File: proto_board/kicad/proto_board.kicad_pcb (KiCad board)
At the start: 2 copper layers, 91 x 96 mm, 1074 parts, among them J1 pcie_98

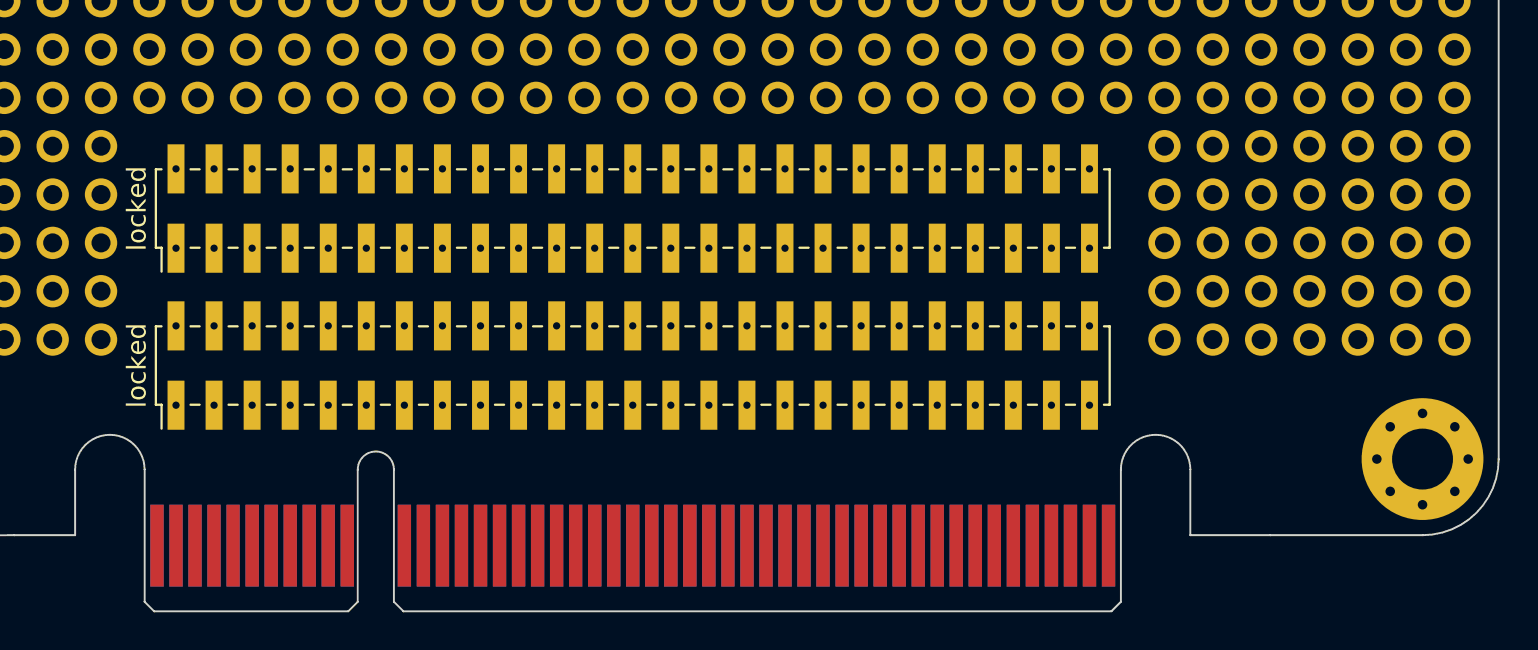
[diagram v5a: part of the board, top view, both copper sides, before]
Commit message: Proto board completed.
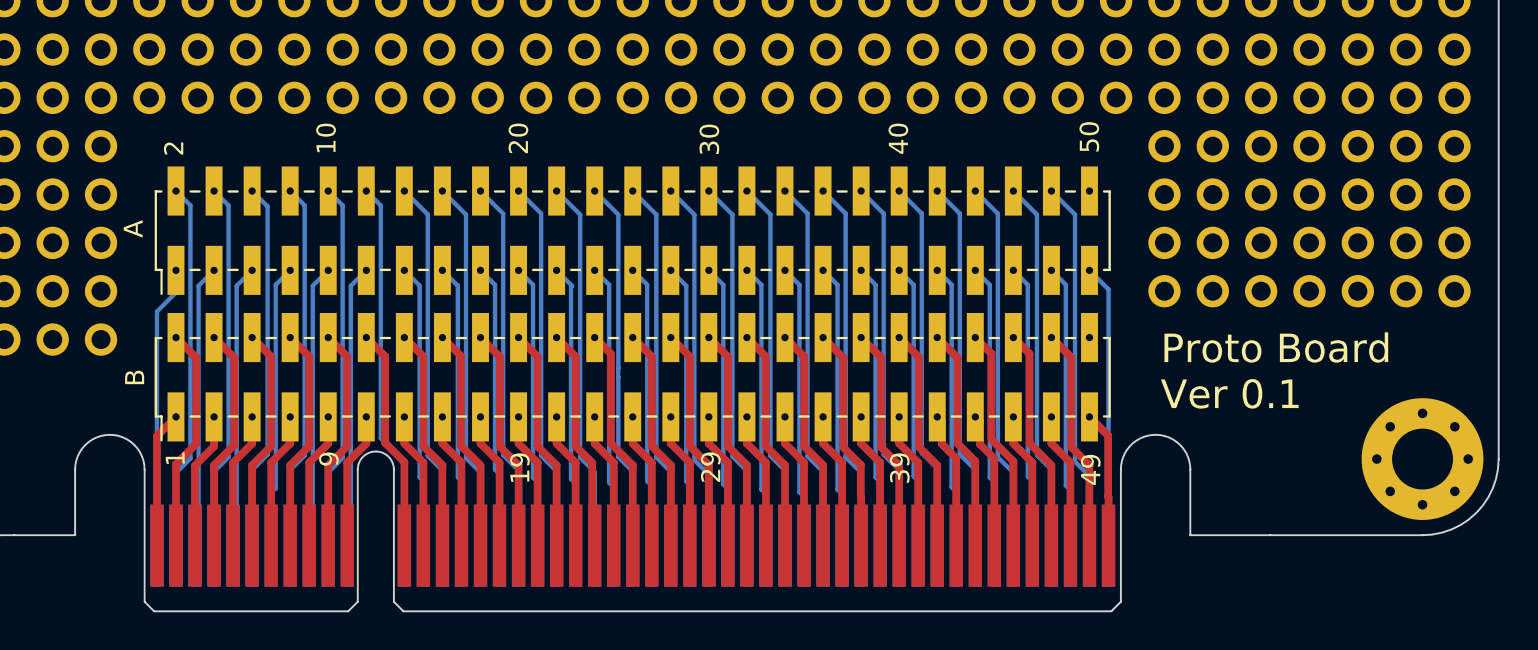
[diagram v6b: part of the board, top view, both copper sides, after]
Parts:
- removed the REF** at (56.7, -14.3)
- removed the REF** at (44.0, -14.3)
- removed the REF** at (54.1, -14.3)
- removed the REF** at (46.5, -14.3)
- removed the REF** at (49.1, -14.3)
- removed the REF** at (51.6, -14.3)
- removed the REF** at (41.4, -14.3)
- moved locked 8.86 mm to (13.5, -12.3)
- moved locked 7.09 mm to (13.5, -20.0)
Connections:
- locked pad 12: /A -> /A12
- locked pad 13: /A -> /A13
- locked pad 14: /A -> /A14
- locked pad 15: /A -> /A15
- locked pad 16: /A -> /A16
- locked pad 17: /A -> /A17
- locked pad 18: /A -> /A18
- locked pad 19: /A -> /A19
- locked pad 20: /A -> /A20
- locked pad 21: /A -> /A21
- locked pad 22: /A -> /A22
- locked pad 23: /A -> /A23
- locked pad 24: /A -> /A24
- locked pad 25: /A -> /A25
- locked pad 26: /A -> /A26
- locked pad 27: /A -> /A27
- locked pad 28: /A -> /A28
- locked pad 29: /A -> /A29
- locked pad 30: /A -> /A30
- locked pad 31: /A -> /A31
- locked pad 32: /A -> /A32
- locked pad 33: /A -> /A33
- locked pad 34: /A -> /A34
- locked pad 35: /A -> /A35
- locked pad 36: /A -> /A36
- locked pad 37: /A -> /A37
- locked pad 38: /A -> /A38
- locked pad 39: /A -> /A39
- locked pad 40: /A -> /A40
- locked pad 41: /A -> /A41
- locked pad 42: /A -> /A42
- locked pad 43: /A -> /A43
- locked pad 44: /A -> /A44
- locked pad 45: /A -> /A45
- locked pad 46: /A -> /A46
- locked pad 47: /A -> /A47
- locked pad 48: /A -> /A48
- locked pad 49: /A -> /A49
- locked pad 50: /A -> unconnected-(J3-Pin_50-Pad50)
- locked pad 12: /B -> /B12
- locked pad 13: /B -> /B13
- locked pad 14: /B -> /B14
- locked pad 15: /B -> /B15
- locked pad 16: /B -> /B16
- locked pad 17: /B -> /B17
- locked pad 18: /B -> /B18
- locked pad 19: /B -> /B19
- locked pad 20: /B -> /B20
- locked pad 21: /B -> /B21
- locked pad 22: /B -> /B22
- locked pad 23: /B -> /B23
- locked pad 24: /B -> /B24
- locked pad 25: /B -> /B25
- locked pad 26: /B -> /B26
- locked pad 27: /B -> /B27
- locked pad 28: /B -> /B28
- locked pad 29: /B -> /B29
- locked pad 30: /B -> /B30
- locked pad 31: /B -> /B31
- locked pad 32: /B -> /B32
- locked pad 33: /B -> /B33
- locked pad 34: /B -> /B34
- locked pad 35: /B -> /B35
- locked pad 36: /B -> /B36
- locked pad 37: /B -> /B37
- locked pad 38: /B -> /B38
- locked pad 39: /B -> /B39
- locked pad 40: /B -> /B40
- locked pad 41: /B -> /B41
- locked pad 42: /B -> /B42
- locked pad 43: /B -> /B43
- locked pad 44: /B -> /B44
- locked pad 45: /B -> /B45
- locked pad 46: /B -> /B46
- locked pad 47: /B -> /B47
- locked pad 48: /B -> /B48
- locked pad 49: /B -> /B49
- locked pad 50: /B -> unconnected-(J2-Pin_50-Pad50)
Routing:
- net /A24: track 0.00 -> 19.5 mm
- net /A48: track 0.00 -> 19.5 mm
- net /A46: track 0.00 -> 19.5 mm
- net /A26: track 0.00 -> 19.5 mm
- net /A22: track 0.00 -> 19.5 mm
- net /A44: track 0.00 -> 19.5 mm
- net /A42: track 0.00 -> 19.5 mm
- net /A40: track 0.00 -> 19.5 mm
- net /A38: track 0.00 -> 19.5 mm
- net /A36: track 0.00 -> 19.5 mm
- net /A34: track 0.00 -> 19.5 mm
- net /A32: track 0.00 -> 19.5 mm
- net /A30: track 0.00 -> 19.5 mm
- net /A28: track 0.00 -> 19.5 mm
- net /A20: track 0.00 -> 19.5 mm
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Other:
- board text added: "1"
- board text added: "10"
- board text added: "19"
- board text added: "2"
- board text added: "20"
- board text added: "29"
- board text added: "30"
- board text added: "39"
- board text added: "40"
- board text added: "49"
- board text added: "50"
- board text added: "9"
- board text added: "A"
- board text added: "B"
- board text added: "Proto Board Ver 0.1"

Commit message: Updated the proto board with the assigned power pins.
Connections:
- J1 pad A1: /A1 -> /GND
- J1 pad A2: /A2 -> /GND
- J1 pad A3: /A3 -> /GND
- J1 pad A4: /A4 -> /GND
- J1 pad A48: /A48 -> /VIN-
- J1 pad A49: /A49 -> /VIN-
- J1 pad B1: /B1 -> /+5V
- J1 pad B2: /B2 -> /+5V
- J1 pad B3: /B3 -> /+5V
- J1 pad B4: /B4 -> /+5V
- J1 pad B48: /B48 -> /VIN+
- J1 pad B49: /B49 -> /VIN+
- locked pad 1: /A1 -> /GND
- locked pad 2: /A2 -> /GND
- locked pad 3: /A3 -> /GND
- locked pad 4: /A4 -> /GND
- locked pad 48: /A48 -> /VIN-
- locked pad 49: /A49 -> /VIN-
- locked pad 50: unconnected-(J3-Pin_50-Pad50) -> /VIN-
- locked pad 1: /B1 -> /+5V
- locked pad 2: /B2 -> /+5V
- locked pad 3: /B3 -> /+5V
- locked pad 4: /B4 -> /+5V
- locked pad 48: /B48 -> /VIN+
- locked pad 49: /B49 -> /VIN+
- locked pad 50: unconnected-(J2-Pin_50-Pad50) -> /VIN+
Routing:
- net /GND: track 0.00 -> 52.4 mm
- net /+5V: track 0.00 -> 36.6 mm
- net /VIN-: track 0.00 -> 25.7 mm
- net /VIN+: track 0.00 -> 25.3 mm
- net /A48: track 19.5 -> 0.00 mm
- net /A4: track 19.3 -> 0.00 mm
- net /A2: track 19.3 -> 0.00 mm
- net /A49: track 14.9 -> 0.00 mm
- net /A3: track 14.9 -> 0.00 mm
- net /A1: track 14.9 -> 0.00 mm
- net /B4: track 11.8 -> 0.00 mm
- net /B2: track 11.8 -> 0.00 mm
- net /B48: track 11.8 -> 0.00 mm
- net /B49: track 7.18 -> 0.00 mm
- net /B3: track 7.18 -> 0.00 mm
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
